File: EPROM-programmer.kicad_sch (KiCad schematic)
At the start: 33 parts, among them J1 ZIF-socket, J2 ISP, J3 DAC_A, J4 DAC_B, J5 GND, P1 USB-C, SW1 SW_Push, U1 ATmega1284-P, U2 MCP2221AxP, U3 MCP4812, Y1 20M

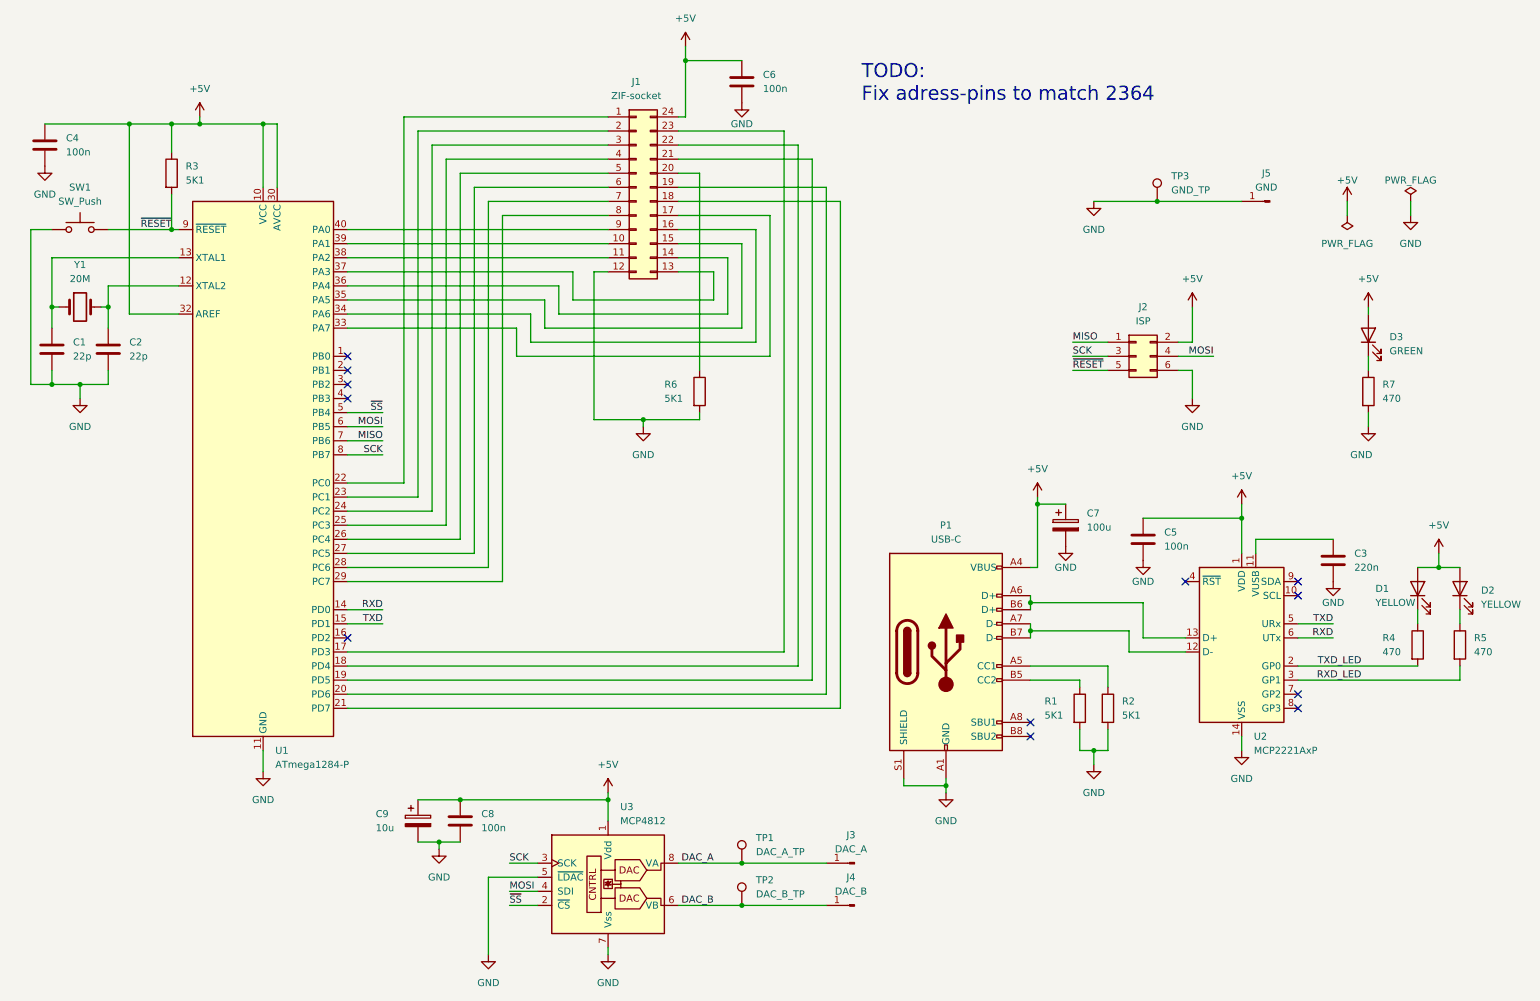
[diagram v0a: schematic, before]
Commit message: Add some net-labels
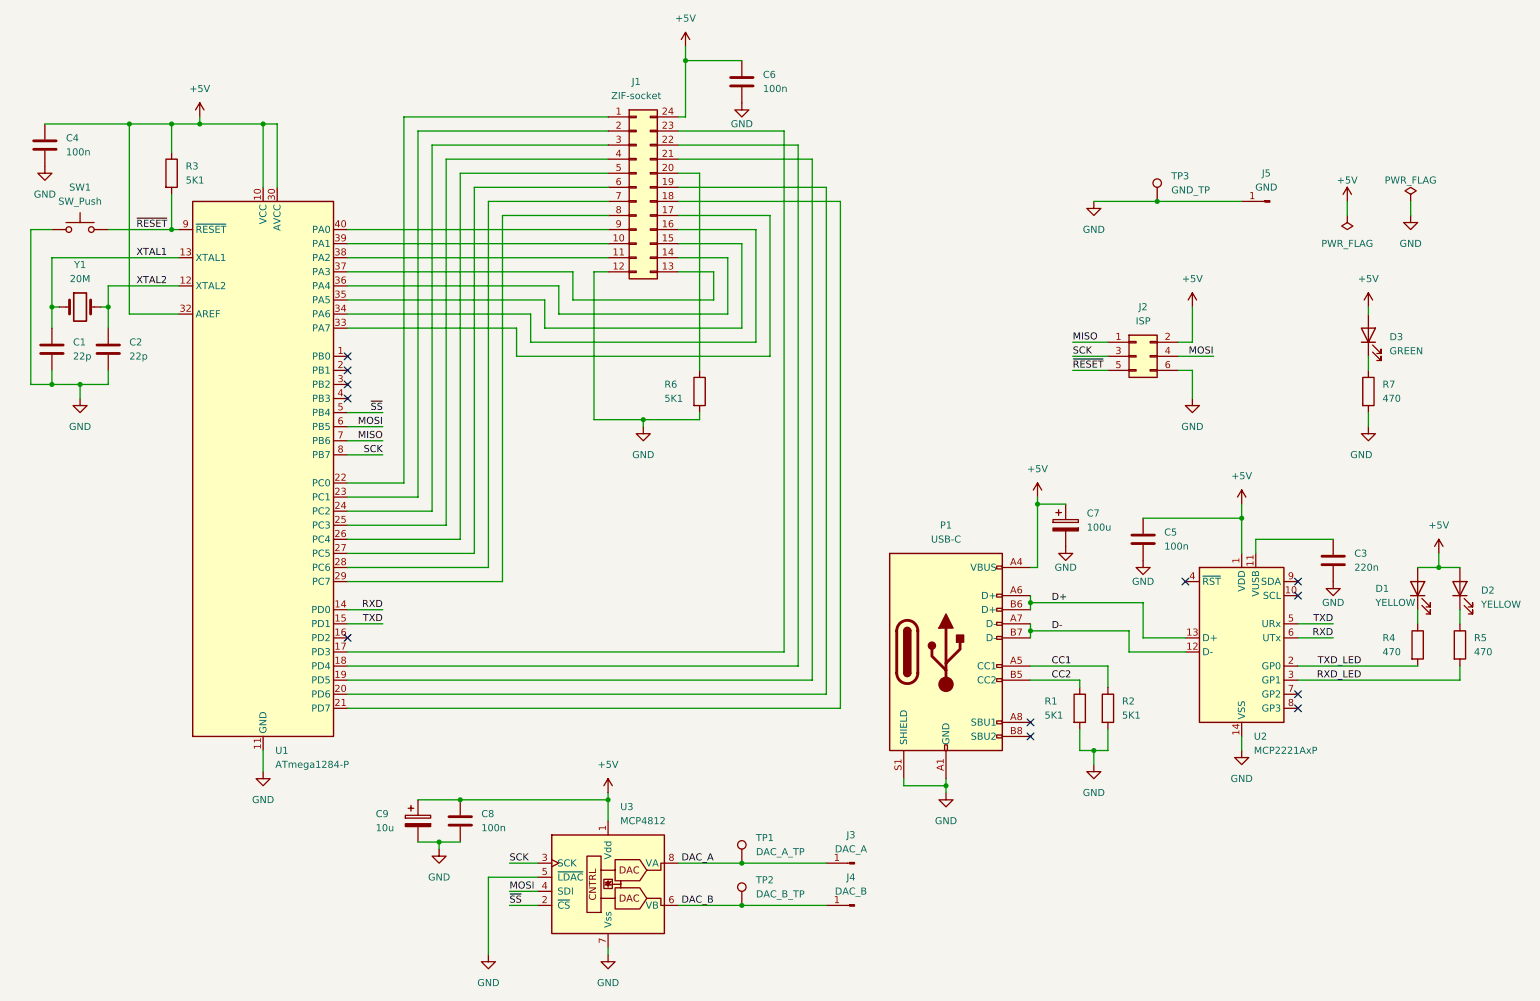
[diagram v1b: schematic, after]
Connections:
- net XTAL2: now reaches C2.1, U1.12 (XTAL2), Y1.2
- net CC1: now reaches P1.A5 (CC1), R2.1
- net XTAL1: now reaches C1.1, U1.13 (XTAL1), Y1.1
- net D-: now reaches P1.A7 (D-), P1.B7 (D-), U2.12 (D-)
- net D+: now reaches P1.A6 (D+), P1.B6 (D+), U2.13 (D+)
- net CC2: now reaches P1.B5 (CC2), R1.1
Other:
- note removed: "TODO: Fix adress-pins to match 2364"
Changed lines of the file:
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@@
     (stroke (width 0) (type default))
   )
-  (wire (pts (xy 41.91 59.69) (xy 19.05 59.69))
+  (wire (pts (xy 19.05 59.69) (xy 41.91 59.69))
     (stroke (width 0) (type default))
   )
@@
     (stroke (width 0) (type default))
   )
-  (text "TODO:\nFix adress-pins to match 2364" (at 165.1 31.75 0)
-    (effects (font (size 2.54 2.54)) (justify left bottom))
+  (label "~{RESET}" (at 34.29 54.61 0) (fields_autoplaced)
+    (effects (font (size 1.27 1.27)) (justify left bottom))
   )
   (label "~{SS}" (at 101.6 176.53 0) (fields_autoplaced)
@@
     (effects (font (size 1.27 1.27)) (justify right bottom))
   )
-  (label "~{RESET}" (at 40.64 54.61 180) (fields_autoplaced)
-    (effects (font (size 1.27 1.27)) (justify right bottom))
+  (label "CC2" (at 199.39 135.89 0) (fields_autoplaced)
+    (effects (font (size 1.27 1.27)) (justify left bottom))
+  )
+  (label "D+" (at 199.39 121.92 0) (fields_autoplaced)
+    (effects (font (size 1.27 1.27)) (justify left bottom))
+  )
+  (label "CC1" (at 199.39 133.35 0) (fields_autoplaced)
+    (effects (font (size 1.27 1.27)) (justify left bottom))
   )
   (label "MISO" (at 78.74 92.71 180) (fields_autoplaced)
@@
     (effects (font (size 1.27 1.27)) (justify right bottom))
   )
+  (label "XTAL2" (at 34.29 64.77 0) (fields_autoplaced)
+    (effects (font (size 1.27 1.27)) (justify left bottom))
+  )
   (label "RXD_LED" (at 255.27 135.89 180) (fields_autoplaced)
     (effects (font (size 1.27 1.27)) (justify right bottom))
@@
     (effects (font (size 1.27 1.27)) (justify right bottom))
   )
+  (label "D-" (at 199.39 127 0) (fields_autoplaced)
+    (effects (font (size 1.27 1.27)) (justify left bottom))
+  )
   (label "MOSI" (at 228.6 77.47 180) (fields_autoplaced)
     (effects (font (size 1.27 1.27)) (justify right bottom))
@@
     (effects (font (size 1.27 1.27)) (justify right bottom))
   )
+  (label "XTAL1" (at 34.29 59.69 0) (fields_autoplaced)
+    (effects (font (size 1.27 1.27)) (justify left bottom))
+  )
   (label "TXD" (at 78.74 125.73 180) (fields_autoplaced)

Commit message: Add missing footprint
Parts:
- C9: footprint (none) -> Capacitor_THT:C_Rect_L4.6mm_W3.0mm_P2.50mm_MKS02_FKP02
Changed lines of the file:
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@@
       (effects (font (size 1.27 1.27)) (justify left))
     )
-    (property "Footprint" "" (at 86.0552 165.1 0)
+    (property "Footprint" "Capacitor_THT:C_Rect_L4.6mm_W3.0mm_P2.50mm_MKS02_FKP02" (at 86.0552 165.1 0)
       (effects (font (size 1.27 1.27)) hide)
     )

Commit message: Change to socket footprints
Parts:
- U1: footprint Package_DIP:DIP-40_W15.24mm -> Package_DIP:DIP-40_W15.24mm_Socket
- U2: footprint Package_DIP:DIP-14_W7.62mm -> Package_DIP:DIP-14_W7.62mm_Socket
- U3: footprint Package_DIP:DIP-8_W7.62mm -> Package_DIP:DIP-8_W7.62mm_Socket
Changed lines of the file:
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@@
       (effects (font (size 1.27 1.27)) (justify left))
     )
-    (property "Footprint" "Package_DIP:DIP-14_W7.62mm" (at 233.68 105.41 0)
+    (property "Footprint" "Package_DIP:DIP-14_W7.62mm_Socket" (at 233.68 105.41 0)
       (effects (font (size 1.27 1.27)) hide)
     )
@@
       (effects (font (size 1.27 1.27)) (justify left))
     )
-    (property "Footprint" "Package_DIP:DIP-40_W15.24mm" (at 57.15 97.79 0)
+    (property "Footprint" "Package_DIP:DIP-40_W15.24mm_Socket" (at 57.15 97.79 0)
       (effects (font (size 1.27 1.27) italic) hide)
     )
@@
       (effects (font (size 1.27 1.27)) (justify left))
     )
-    (property "Footprint" "Package_DIP:DIP-8_W7.62mm" (at 139.7 179.07 0)
-      (effects (font (size 1.27 1.27)) hide)
-    )
+    (property "Footprint" "Package_DIP:DIP-8_W7.62mm_Socket" (at 139.7 179.07 0)
+      (effects (font (size 1.27 1.27)) hide)
+    )

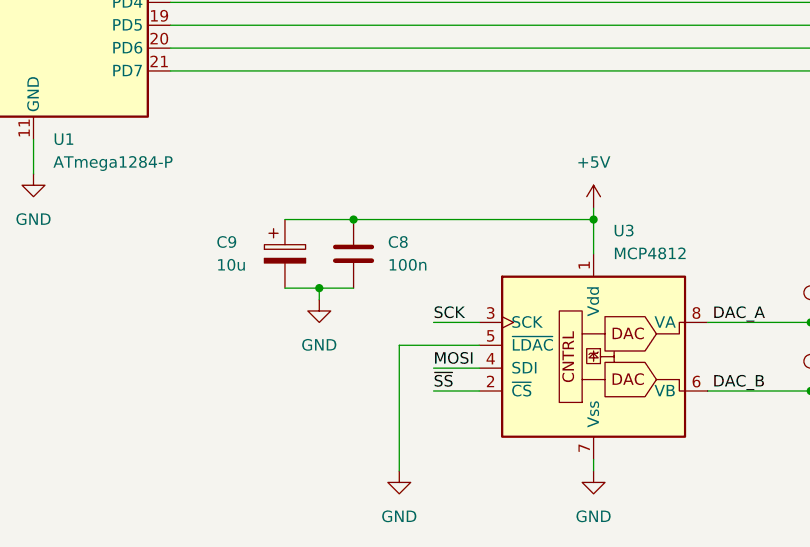
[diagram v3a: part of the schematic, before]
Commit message: Add pull-up for select-line for DAC
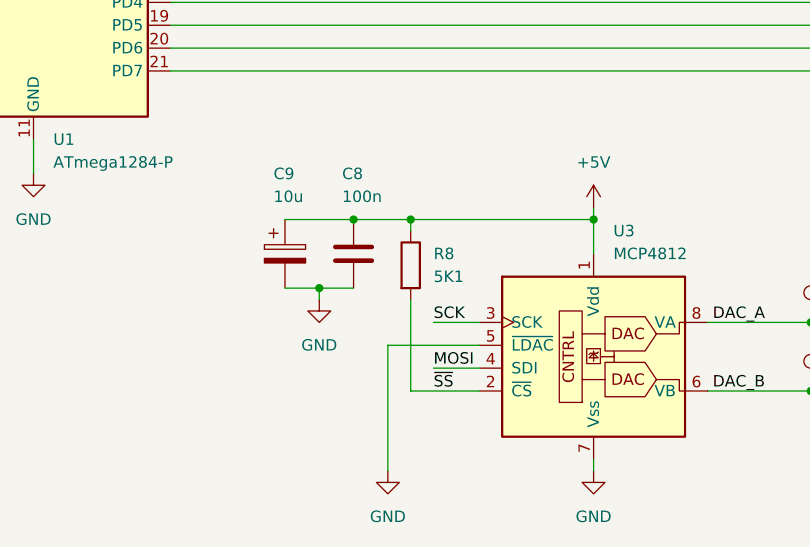
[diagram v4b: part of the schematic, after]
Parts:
- added R8: 5K1, Resistor_THT:R_Axial_DIN0207_L6.3mm_D2.5mm_P10.16mm_Horizontal, symbol Device:R
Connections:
- net +5V: now also R8.1
- net ~{SS}: now also R8.2
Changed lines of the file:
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@@
   (junction (at 269.24 115.57) (diameter 0) (color 0 0 0 0)
+  )
+  (junction (at 99.06 157.48) (diameter 0) (color 0 0 0 0)
   )
   (junction (at 180.34 154.94) (diameter 0) (color 0 0 0 0)
@@
     (stroke (width 0) (type default))
   )
-  (wire (pts (xy 101.6 176.53) (xy 106.68 176.53))
+  (wire (pts (xy 99.06 176.53) (xy 106.68 176.53))
     (stroke (width 0) (type default))
   )
@@
     (stroke (width 0) (type default))
   )
-  (wire (pts (xy 92.71 157.48) (xy 119.38 157.48))
+  (wire (pts (xy 92.71 157.48) (xy 99.06 157.48))
     (stroke (width 0) (type default))
   )
@@
     (stroke (width 0) (type default))
   )
-  (wire (pts (xy 97.79 171.45) (xy 106.68 171.45))
+  (wire (pts (xy 99.06 166.37) (xy 99.06 176.53))
+    (stroke (width 0) (type default))
+  )
+  (wire (pts (xy 96.52 171.45) (xy 106.68 171.45))
     (stroke (width 0) (type default))
   )
@@
     (stroke (width 0) (type default))
   )
+  (wire (pts (xy 99.06 157.48) (xy 119.38 157.48))
+    (stroke (width 0) (type default))
+  )
   (wire (pts (xy 215.9 128.27) (xy 223.52 128.27))
     (stroke (width 0) (type default))
@@
     (stroke (width 0) (type default))
   )
+  (wire (pts (xy 99.06 158.75) (xy 99.06 157.48))
+    (stroke (width 0) (type default))
+  )
   (wire (pts (xy 92.71 110.49) (xy 92.71 44.45))
     (stroke (width 0) (type default))
@@
     (stroke (width 0) (type default))
   )
-  (wire (pts (xy 97.79 171.45) (xy 97.79 185.42))
+  (wire (pts (xy 96.52 171.45) (xy 96.52 185.42))
     (stroke (width 0) (type default))
   )
@@
   )
   (symbol (lib_id "Device:C") (at 92.71 161.29 0) (unit 1)
-    (in_bom yes) (on_board yes) (dnp no) (fields_autoplaced)
-    (property "Reference" "C8" (at 96.52 160.02 0)
-      (effects (font (size 1.27 1.27)) (justify left))
-    )
-    (property "Value" "100n" (at 96.52 162.56 0)
+    (in_bom yes) (on_board yes) (dnp no)
+    (property "Reference" "C8" (at 91.44 152.4 0)
+      (effects (font (size 1.27 1.27)) (justify left))
+    )
+    (property "Value" "100n" (at 91.44 154.94 0)
       (effects (font (size 1.27 1.27)) (justify left))
     )
@@
     )
   )
-  (symbol (lib_id "power:GND") (at 97.79 185.42 0) (unit 1)
-    (in_bom yes) (on_board yes) (dnp no) (fields_autoplaced)
-    (property "Reference" "#PWR025" (at 97.79 191.77 0)
-      (effects (font (size 1.27 1.27)) hide)
-    )
-    (property "Value" "GND" (at 97.79 190.5 0)
-      (effects (font (size 1.27 1.27)))
-    )
-    (property "Footprint" "" (at 97.79 185.42 0)
-      (effects (font (size 1.27 1.27)) hide)
-    )
-    (property "Datasheet" "" (at 97.79 185.42 0)
+  (symbol (lib_id "power:GND") (at 96.52 185.42 0) (unit 1)
+    (in_bom yes) (on_board yes) (dnp no) (fields_autoplaced)
+    (property "Reference" "#PWR025" (at 96.52 191.77 0)
+      (effects (font (size 1.27 1.27)) hide)
+    )
+    (property "Value" "GND" (at 96.52 190.5 0)
+      (effects (font (size 1.27 1.27)))
+    )
+    (property "Footprint" "" (at 96.52 185.42 0)
+      (effects (font (size 1.27 1.27)) hide)
+    )
+    (property "Datasheet" "" (at 96.52 185.42 0)
       (effects (font (size 1.27 1.27)) hide)
     )
@@
   (symbol (lib_id "Device:C_Polarized") (at 85.09 161.29 0) (unit 1)
     (in_bom yes) (on_board yes) (dnp no)
-    (property "Reference" "C9" (at 77.47 160.02 0)
-      (effects (font (size 1.27 1.27)) (justify left))
-    )
-    (property "Value" "10u" (at 77.47 162.56 0)
+    (property "Reference" "C9" (at 83.82 152.4 0)
+      (effects (font (size 1.27 1.27)) (justify left))
+    )
+    (property "Value" "10u" (at 83.82 154.94 0)
       (effects (font (size 1.27 1.27)) (justify left))
     )
@@
         )
       )
+    )
+  )
+  (symbol (lib_id "Device:R") (at 99.06 162.56 0) (unit 1)
+    (in_bom yes) (on_board yes) (dnp no)
+    (property "Reference" "R8" (at 101.6 161.29 0)
+      (effects (font (size 1.27 1.27)) (justify left))
+    )
+    (property "Value" "5K1" (at 101.6 163.83 0)
+      (effects (font (size 1.27 1.27)) (justify left))
+    )
+    (property "Footprint" "Resistor_THT:R_Axial_DIN0207_L6.3mm_D2.5mm_P10.16mm_Horizontal" (at 97.282 162.56 90)
+      (effects (font (size 1.27 1.27)) hide)
+    )
+    (property "Datasheet" "~" (at 99.06 162.56 0)
+      (effects (font (size 1.27 1.27)) hide)
+    )
+    (pin "1")
+    (pin "2")
+    (instances
+      (project "EPROM-programmer"
+        (path "/8c5576b1-cb3e-4456-837b-2f47818a03ab"
+          (reference "R8") (unit 1)
+        )
+      )
